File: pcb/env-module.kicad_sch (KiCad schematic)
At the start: 8 parts

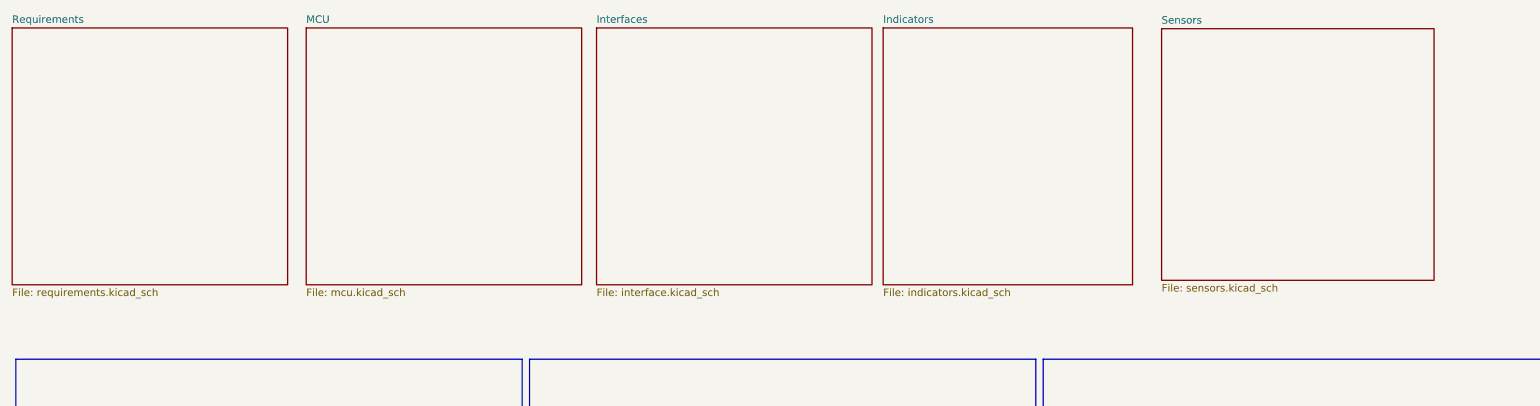
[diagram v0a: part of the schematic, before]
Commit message: Updated license and implemented RP2040
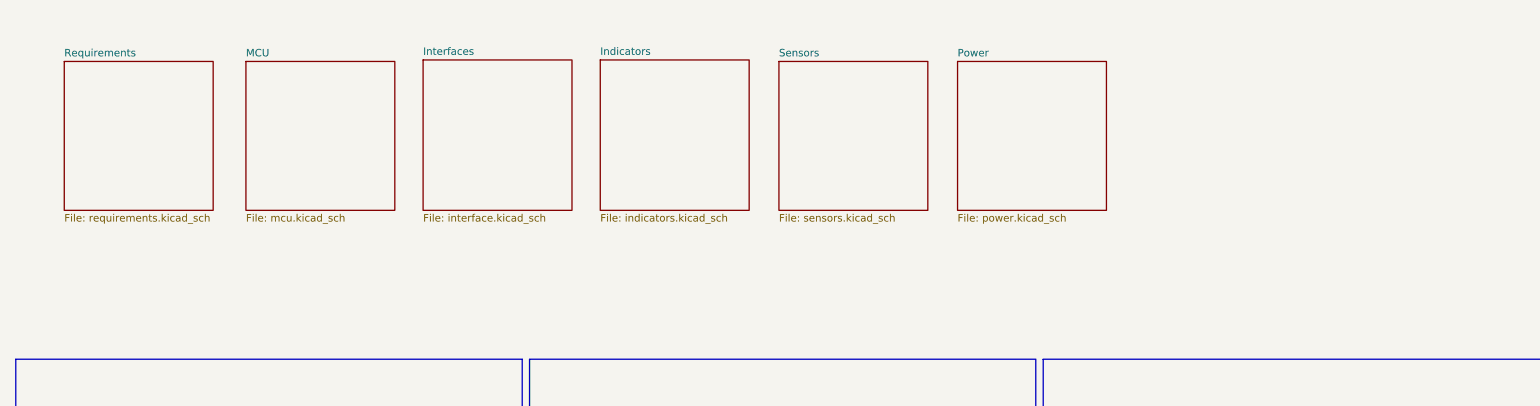
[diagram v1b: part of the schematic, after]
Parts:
- LOGO1: renamed from LOGO4; footprint CRGM Logos:CRGM Logo 5mm -> CRGM Logos:CRGM Logo 10mm
- LOGO2: footprint CRGM Logos:Aquarius Logo 8mm -> CRGM Logos:Aquarius Logo 5mm
- LOGO3: renamed from LOGO1; footprint CRGM Logos:Aquarius Logo 8mm -> CRGM Logos:Aquarius Logo 5mm
- renumbered LOGO3 to LOGO4
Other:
- added sheet Power (power.kicad_sch)
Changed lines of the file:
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@@
 		(dnp no)
 		(fields_autoplaced yes)
-		(property "Reference" "LOGO1"
+		(property "Reference" "LOGO3"
 			(at 260.604 176.53 0)
 			(effects
@@
 			)
 		)
-		(property "Footprint" "CRGM Logos:Aquarius Logo 8mm"
+		(property "Footprint" "CRGM Logos:Aquarius Logo 5mm"
 			(at 261.874 178.308 0)
 			(effects
@@
 			(project ""
 				(path "/445c1fff-2e1a-48b1-a91f-a137832edebf"
-					(reference "LOGO1")
+					(reference "LOGO3")
 					(unit 1)
 				)
@@
 		(at 271.78 175.26 0)
 		(unit 1)
-		(exclude_from_sim no)
+		(exclude_from_sim yes)
 		(in_bom no)
 		(on_board yes)
 		(dnp no)
 		(fields_autoplaced yes)
-		(property "Reference" "LOGO3"
+		(property "Reference" "LOGO4"
 			(at 271.78 168.275 0)
 			(effects
@@
 			(project ""
 				(path "/445c1fff-2e1a-48b1-a91f-a137832edebf"
-					(reference "LOGO3")
+					(reference "LOGO4")
 					(unit 1)
 				)
@@
 		(on_board yes)
 		(dnp no)
-		(property "Reference" "LOGO4"
+		(property "Reference" "LOGO1"
 			(at 248.92 180.34 0)
 			(effects
@@
 			)
 		)
-		(property "Footprint" "CRGM Logos:CRGM Logo 5mm"
+		(property "Footprint" "CRGM Logos:CRGM Logo 10mm"
 			(at 248.92 182.118 0)
 			(effects
@@
 			(project ""
 				(path "/445c1fff-2e1a-48b1-a91f-a137832edebf"
-					(reference "LOGO4")
+					(reference "LOGO1")
 					(unit 1)
 				)
@@
 			)
 		)
-		(property "Footprint" "CRGM Logos:Aquarius Logo 8mm"
+		(property "Footprint" "CRGM Logos:Aquarius Logo 5mm"
 			(at 239.014 178.308 0)
 			(effects
@@
 	)
 	(sheet
-		(at 212.598 19.812)
-		(size 46.482 42.926)
+		(at 147.32 25.4)
+		(size 25.4 25.4)
 		(exclude_from_sim no)
 		(in_bom yes)
@@
 		)
 		(property "Sheetname" "Sensors"
-			(at 212.598 19.1004 0)
+			(at 147.32 24.6884 0)
 			(effects
 				(font
@@
 		)
 		(property "Sheetfile" "sensors.kicad_sch"
-			(at 212.598 63.3226 0)
+			(at 147.32 51.3846 0)
 			(effects
 				(font
@@
 	)
 	(sheet
-		(at 165.1 19.685)
-		(size 42.545 43.815)
+		(at 116.84 25.146)
+		(size 25.4 25.654)
 		(exclude_from_sim no)
 		(in_bom yes)
@@
 		)
 		(property "Sheetname" "Indicators"
-			(at 165.1 18.9734 0)
+			(at 116.84 24.4344 0)
 			(effects
 				(font
@@
 		)
 		(property "Sheetfile" "indicators.kicad_sch"
-			(at 165.1 64.0846 0)
+			(at 116.84 51.3846 0)
 			(effects
 				(font
@@
 	)
 	(sheet
-		(at 66.675 19.685)
-		(size 46.99 43.815)
+		(at 56.388 25.4)
+		(size 25.4 25.4)
 		(exclude_from_sim no)
 		(in_bom yes)
@@
 		)
 		(property "Sheetname" "MCU"
-			(at 66.675 18.9734 0)
+			(at 56.388 24.6884 0)
 			(effects
 				(font
@@
 		)
 		(property "Sheetfile" "mcu.kicad_sch"
-			(at 66.675 64.0846 0)
+			(at 56.388 51.3846 0)
 			(effects
 				(font
@@
 	)
 	(sheet
-		(at 16.51 19.685)
-		(size 46.99 43.815)
+		(at 25.4 25.4)
+		(size 25.4 25.4)
 		(exclude_from_sim no)
 		(in_bom yes)
@@
 		)
 		(property "Sheetname" "Requirements"
-			(at 16.51 18.9734 0)
+			(at 25.4 24.6884 0)
 			(effects
 				(font
@@
 		)
 		(property "Sheetfile" "requirements.kicad_sch"
-			(at 16.51 64.0846 0)
+			(at 25.4 51.3846 0)
 			(effects
 				(font
@@
 	)
 	(sheet
-		(at 116.205 19.685)
-		(size 46.99 43.815)
+		(at 86.614 25.146)
+		(size 25.4 25.654)
 		(exclude_from_sim no)
 		(in_bom yes)
@@
 		)
 		(property "Sheetname" "Interfaces"
-			(at 116.205 18.9734 0)
+			(at 86.614 24.4344 0)
 			(effects
 				(font
@@
 		)
 		(property "Sheetfile" "interface.kicad_sch"
-			(at 116.205 64.0846 0)
+			(at 86.614 51.3846 0)
 			(effects
 				(font
@@
 				)
 			)
+		)
+	)
+	(sheet
+		(at 177.7915 25.4024)
+		(size 25.4 25.4)
+		(exclude_from_sim no)
+		(in_bom yes)
+		(on_board yes)
+		(dnp no)
+		(fields_autoplaced yes)
+		(stroke
+			(width 0.1524)
+			(type solid)
+		)
+		(fill
+			(color 0 0 0 0.0000)
+		)
+		(property "Sheetname" "Power"
+			(at 177.7915 24.6908 0)
+			(effects
+				(font
+					(size 1.27 1.27)
+				)
+				(justify left bottom)
+			)
+		)
+		(property "Sheetfile" "power.kicad_sch"
+			(at 177.7915 51.387 0)
+			(effects
+				(font
+					(size 1.27 1.27)
+				)
+				(justify left top)
+			)
+		)
+		(instances
+			(project "env-module"
+				(path "/445c1fff-2e1a-48b1-a91f-a137832edebf"
+					(page "7")
+				)
+			)
